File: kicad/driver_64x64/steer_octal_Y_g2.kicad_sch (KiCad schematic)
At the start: 66 parts

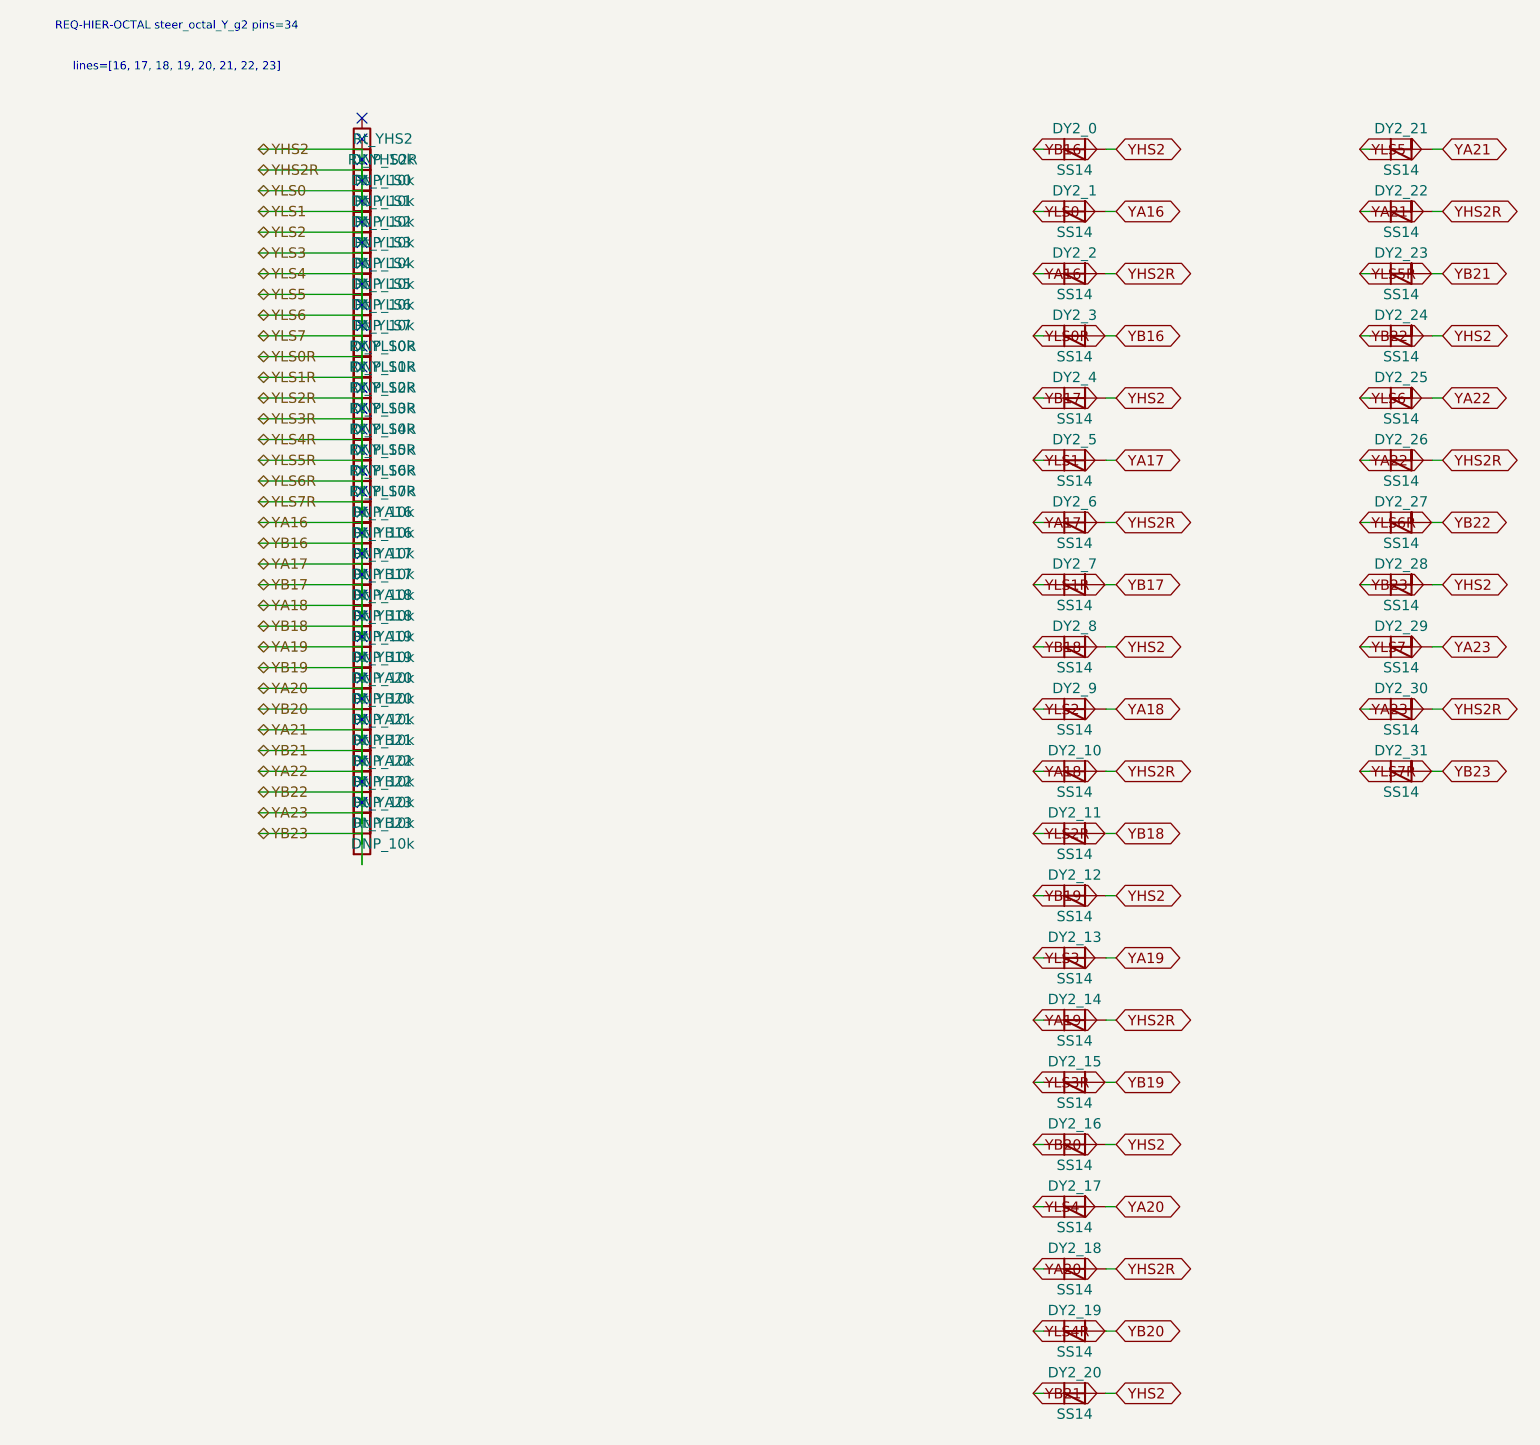
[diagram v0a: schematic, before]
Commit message: logical seperation into host and multiple decode/drive/steering boards
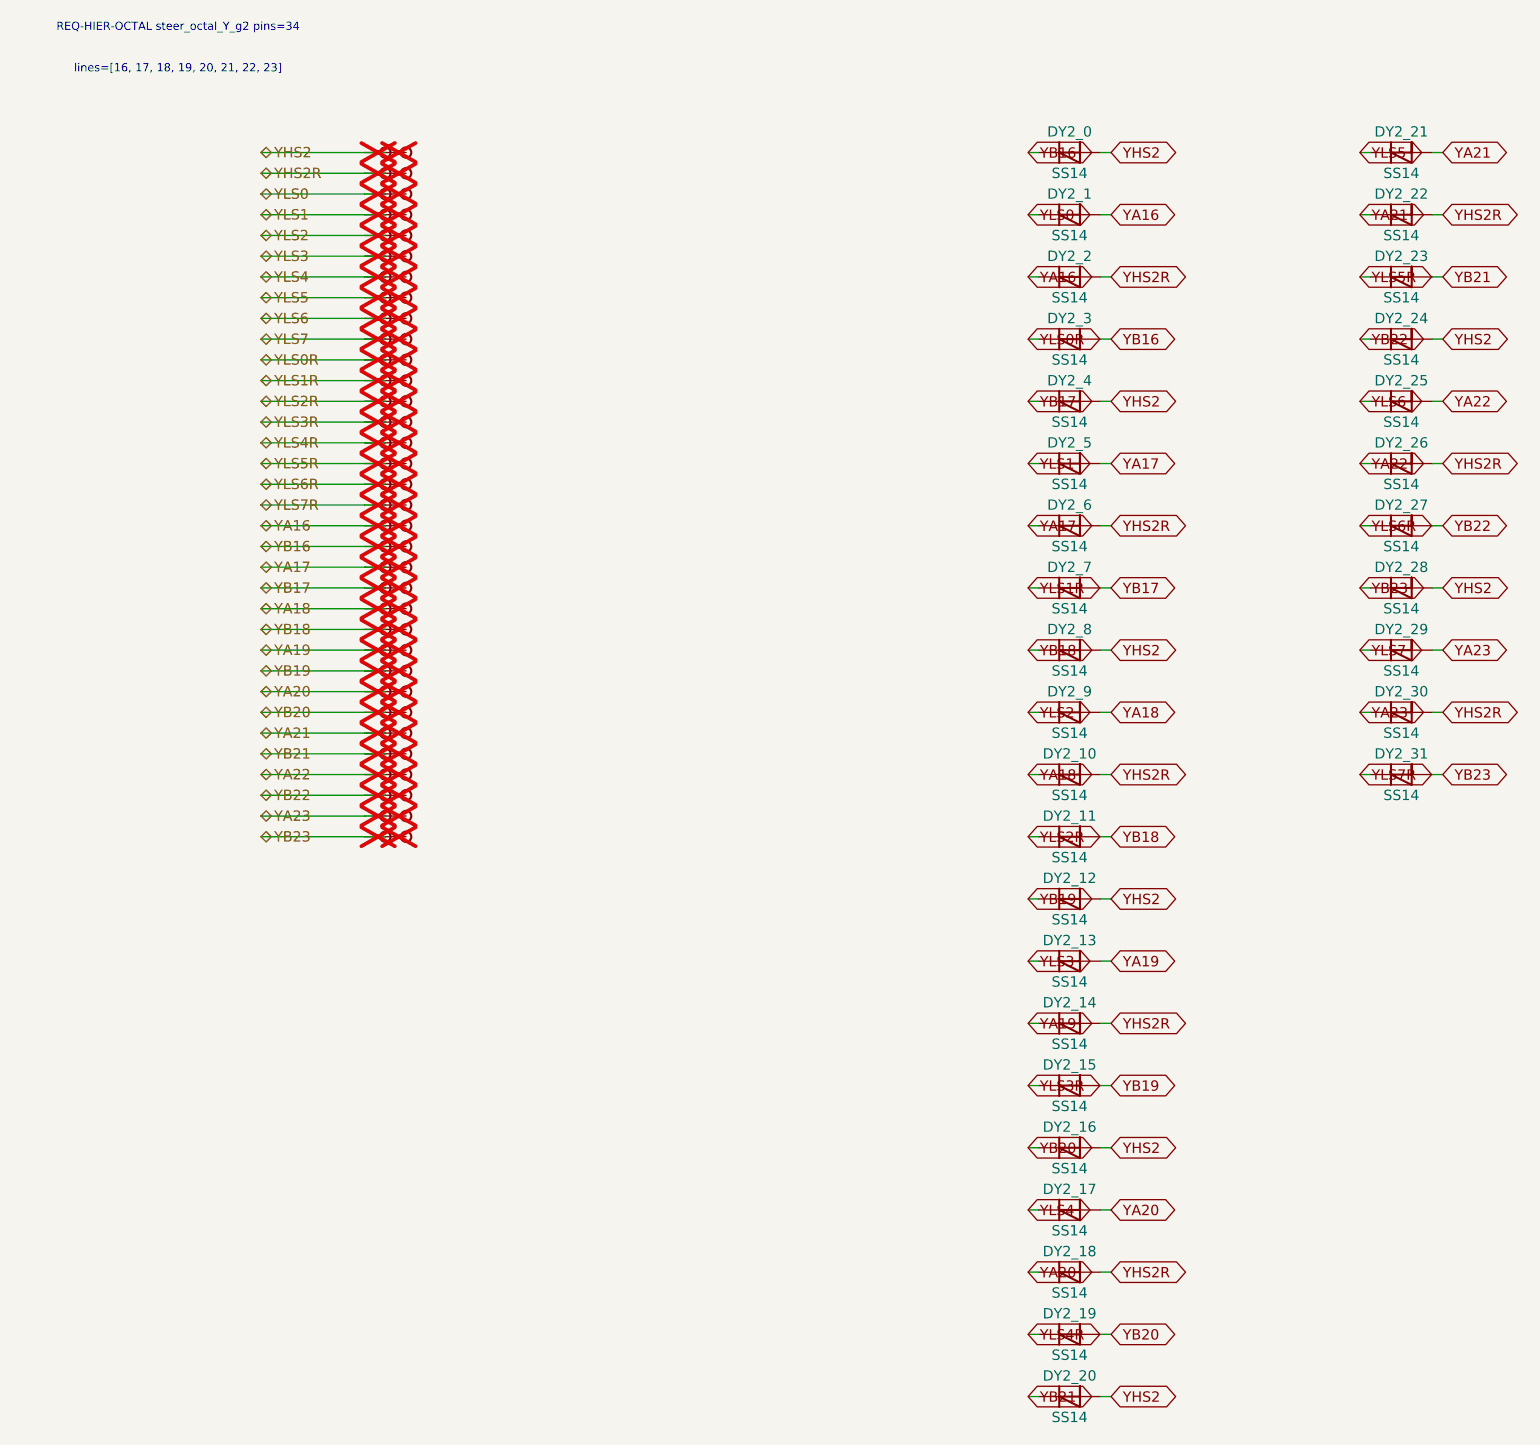
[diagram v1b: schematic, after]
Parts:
- removed Rt_YA16, Rt_YA17, Rt_YA18, Rt_YA19, Rt_YA20, Rt_YA21, Rt_YA22, Rt_YA23, Rt_YB16, Rt_YB17, Rt_YB18, Rt_YB19, Rt_YB20, Rt_YB21, Rt_YB22, Rt_YB23, Rt_YHS2, Rt_YHS2R, Rt_YLS0, Rt_YLS0R, Rt_YLS1, Rt_YLS1R, Rt_YLS2, Rt_YLS2R, Rt_YLS3, Rt_YLS3R, Rt_YLS4, Rt_YLS4R, Rt_YLS5, Rt_YLS5R, Rt_YLS6, Rt_YLS6R, Rt_YLS7, Rt_YLS7R: DNP_10k, symbol Device:R
- added TP_YA16, TP_YA16b, TP_YA17, TP_YA17b, TP_YA18, TP_YA18b, TP_YA19, TP_YA19b, TP_YA20, TP_YA20b, TP_YA21, TP_YA21b, TP_YA22, TP_YA22b, TP_YA23, TP_YA23b, TP_YB16, TP_YB16b, TP_YB17, TP_YB17b, TP_YB18, TP_YB18b, TP_YB19, TP_YB19b, TP_YB20, TP_YB20b, TP_YB21, TP_YB21b, TP_YB22, TP_YB22b, TP_YB23, TP_YB23b, TP_YHS2, TP_YHS2R, TP_YHS2Rb, TP_YHS2b, TP_YLS0, TP_YLS0R, TP_YLS0Rb, TP_YLS0b, TP_YLS1, TP_YLS1R, TP_YLS1Rb, TP_YLS1b, TP_YLS2, TP_YLS2R, TP_YLS2Rb, TP_YLS2b, TP_YLS3, TP_YLS3R, TP_YLS3Rb, TP_YLS3b, TP_YLS4, TP_YLS4R, TP_YLS4Rb, TP_YLS4b, TP_YLS5, TP_YLS5R, TP_YLS5Rb, TP_YLS5b, TP_YLS6, TP_YLS6R, TP_YLS6Rb, TP_YLS6b, TP_YLS7, TP_YLS7R, TP_YLS7Rb, TP_YLS7b: Stub, symbol CMR:Stub
- DY2_0, DY2_1, DY2_10, DY2_11, DY2_12, DY2_13, DY2_14, DY2_15, DY2_16, DY2_17, DY2_18, DY2_19, DY2_2, DY2_20, DY2_21, DY2_22, DY2_23, DY2_24, DY2_25, DY2_26, DY2_27, DY2_28, DY2_29, DY2_3, DY2_30, DY2_31, DY2_4, DY2_5, DY2_6, DY2_7, DY2_8, DY2_9: symbol Device:D_Schottky -> CMR:D_Schottky
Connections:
- net YA16: now also TP_YA16.1, TP_YA16b.1; no longer DY2_0.1 (K), DY2_0.2 (A), DY2_1.1 (K), DY2_10.1 (K), DY2_10.2 (A), DY2_11.1 (K), DY2_11.2 (A), DY2_12.1 (K), DY2_12.2 (A), DY2_13.1 (K), DY2_13.2 (A), DY2_14.1 (K), DY2_14.2 (A), DY2_15.1 (K), DY2_15.2 (A), DY2_16.1 (K), DY2_16.2 (A), DY2_17.1 (K), DY2_17.2 (A), DY2_18.1 (K), DY2_18.2 (A), DY2_19.1 (K), DY2_19.2 (A), DY2_2.2 (A), DY2_20.1 (K), DY2_20.2 (A), DY2_21.1 (K), DY2_21.2 (A), DY2_22.1 (K), DY2_22.2 (A), DY2_23.1 (K), DY2_23.2 (A), DY2_24.1 (K), DY2_24.2 (A), DY2_25.1 (K), DY2_25.2 (A), DY2_26.1 (K), DY2_26.2 (A), DY2_27.1 (K), DY2_27.2 (A), DY2_28.1 (K), DY2_28.2 (A), DY2_29.1 (K), DY2_29.2 (A), DY2_3.1 (K), DY2_3.2 (A), DY2_30.1 (K), DY2_30.2 (A), DY2_31.1 (K), DY2_31.2 (A), DY2_4.1 (K), DY2_4.2 (A), DY2_5.1 (K), DY2_5.2 (A), DY2_6.1 (K), DY2_6.2 (A), DY2_7.1 (K), DY2_7.2 (A), DY2_8.1 (K), DY2_8.2 (A), DY2_9.1 (K), DY2_9.2 (A)
- new net YA17: DY2_5.2 (A), DY2_6.1 (K), TP_YA17.1, TP_YA17b.1
- new net YA18: DY2_10.1 (K), DY2_9.2 (A), TP_YA18.1, TP_YA18b.1
- new net YA19: DY2_13.2 (A), DY2_14.1 (K), TP_YA19.1, TP_YA19b.1
- new net YA20: DY2_17.2 (A), DY2_18.1 (K), TP_YA20.1, TP_YA20b.1
- new net YA21: DY2_21.2 (A), DY2_22.1 (K), TP_YA21.1, TP_YA21b.1
- new net YA22: DY2_25.2 (A), DY2_26.1 (K), TP_YA22.1, TP_YA22b.1
- new net YA23: DY2_29.2 (A), DY2_30.1 (K), TP_YA23.1, TP_YA23b.1
- new net YB16: DY2_0.1 (K), DY2_3.2 (A), TP_YB16.1, TP_YB16b.1
- new net YB17: DY2_4.1 (K), DY2_7.2 (A), TP_YB17.1, TP_YB17b.1
- new net YB18: DY2_11.2 (A), DY2_8.1 (K), TP_YB18.1, TP_YB18b.1
- new net YB19: DY2_12.1 (K), DY2_15.2 (A), TP_YB19.1, TP_YB19b.1
- new net YB20: DY2_16.1 (K), DY2_19.2 (A), TP_YB20.1, TP_YB20b.1
- new net YB21: DY2_20.1 (K), DY2_23.2 (A), TP_YB21.1, TP_YB21b.1
- new net YB22: DY2_24.1 (K), DY2_27.2 (A), TP_YB22.1, TP_YB22b.1
- new net YB23: DY2_28.1 (K), DY2_31.2 (A), TP_YB23.1, TP_YB23b.1
- new net YHS2: DY2_0.2 (A), DY2_12.2 (A), DY2_16.2 (A), DY2_20.2 (A), DY2_24.2 (A), DY2_28.2 (A), DY2_4.2 (A), DY2_8.2 (A), TP_YHS2.1, TP_YHS2b.1
- new net YHS2R: DY2_10.2 (A), DY2_14.2 (A), DY2_18.2 (A), DY2_2.2 (A), DY2_22.2 (A), DY2_26.2 (A), DY2_30.2 (A), DY2_6.2 (A), TP_YHS2R.1, TP_YHS2Rb.1
- new net YLS0: DY2_1.1 (K), TP_YLS0.1, TP_YLS0b.1
- new net YLS0R: DY2_3.1 (K), TP_YLS0R.1, TP_YLS0Rb.1
- new net YLS1: DY2_5.1 (K), TP_YLS1.1, TP_YLS1b.1
- new net YLS1R: DY2_7.1 (K), TP_YLS1R.1, TP_YLS1Rb.1
- new net YLS2: DY2_9.1 (K), TP_YLS2.1, TP_YLS2b.1
- new net YLS2R: DY2_11.1 (K), TP_YLS2R.1, TP_YLS2Rb.1
- new net YLS3: DY2_13.1 (K), TP_YLS3.1, TP_YLS3b.1
- new net YLS3R: DY2_15.1 (K), TP_YLS3R.1, TP_YLS3Rb.1
- new net YLS4: DY2_17.1 (K), TP_YLS4.1, TP_YLS4b.1
- new net YLS4R: DY2_19.1 (K), TP_YLS4R.1, TP_YLS4Rb.1
- new net YLS5: DY2_21.1 (K), TP_YLS5.1, TP_YLS5b.1
- new net YLS5R: DY2_23.1 (K), TP_YLS5R.1, TP_YLS5Rb.1
- new net YLS6: DY2_25.1 (K), TP_YLS6.1, TP_YLS6b.1
- new net YLS6R: DY2_27.1 (K), TP_YLS6R.1, TP_YLS6Rb.1
- new net YLS7: DY2_29.1 (K), TP_YLS7.1, TP_YLS7b.1
- new net YLS7R: DY2_31.1 (K), TP_YLS7R.1, TP_YLS7Rb.1
- no-connect marks 34 -> 0
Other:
- moved on the sheet: DY2_0, DY2_1, DY2_10, DY2_11, DY2_12, DY2_13, DY2_14, DY2_15, DY2_16, DY2_17, DY2_18, DY2_19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
